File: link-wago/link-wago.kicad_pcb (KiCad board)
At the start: 4 copper layers, 70 x 29 mm, 37 parts, among them J101 2x05_Horizontal, J102 NE8FAH, J103 JAE_DX07S016JA3, J104 2x05_Horizontal, J105 NE8FAH, J106 Conn_01x01, J107 Conn_01x01, J108 WAGO-2065, J109 WAGO-2065, J110 WAGO-2065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

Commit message: Refresh
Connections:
- net /+24V-Supply renamed /+24V-Link
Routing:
- net GND: vias 29 -> 28

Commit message: Update
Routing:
- net GND: track 5.90 -> 12.1 mm, vias 28 -> 46
- net /Plug-RX-B: track 26.4 -> 25.7 mm
- net /USB-: track 36.8 -> 36.4 mm, vias 1 -> 2
- net /USB+: track 28.7 -> 28.5 mm, vias 1 -> 2
- added copper zone on B.Cu, net +5V
- removed copper zone on In2.Cu, net +24V
- removed copper zone on In2.Cu, net +5V
- removed copper zone on In2.Cu, net /+24V-Link

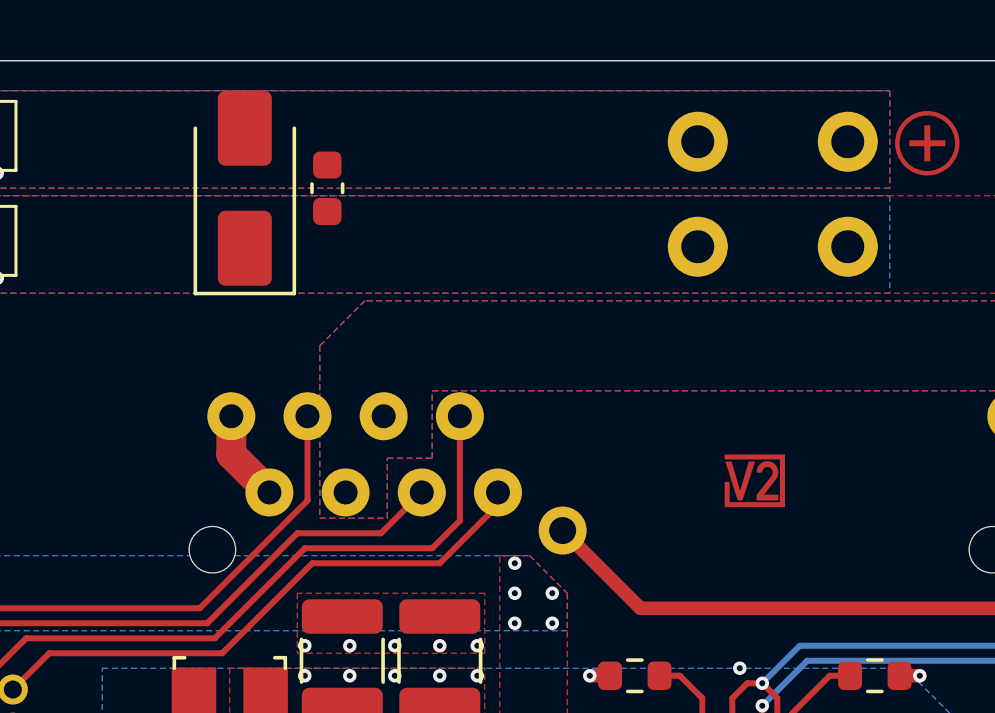
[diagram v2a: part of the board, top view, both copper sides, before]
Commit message: Update power symbols
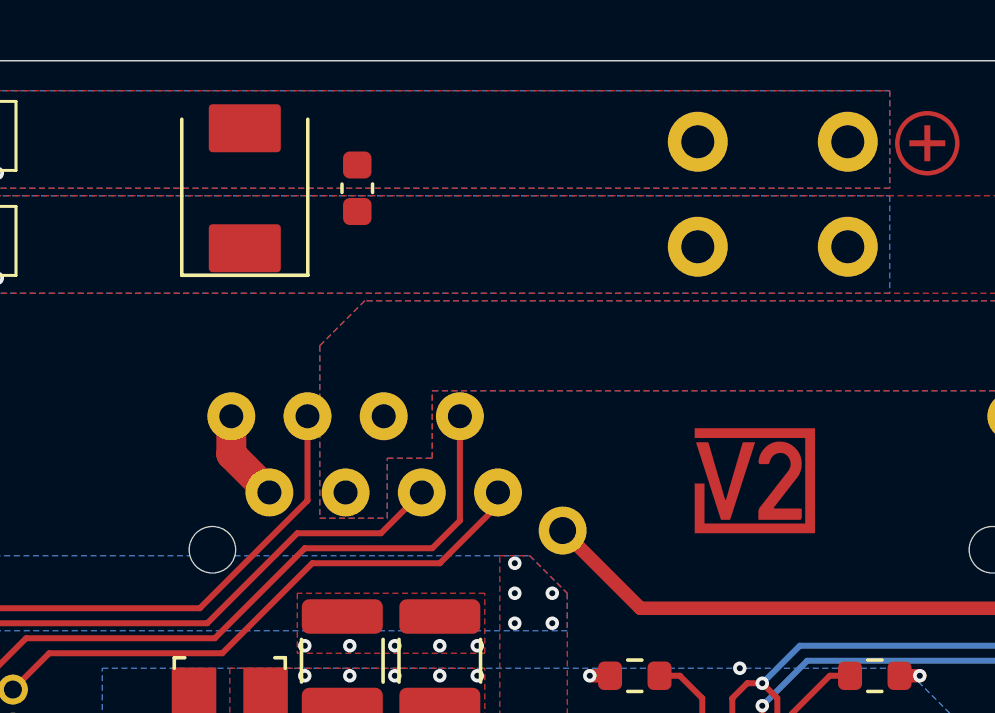
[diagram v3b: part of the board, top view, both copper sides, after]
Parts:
- C101, C502, C505: footprint Capacitor_SMD:C_0603_1608Metric -> V2_Capacitor_SMD:C_0603
- C501, C503, C504: footprint Capacitor_SMD:C_1210_3225Metric -> V2_Capacitor_SMD:C_1210
- FID101, FID102, FID103: value Fiducial -> Fiducial_Paste
- ICON102: footprint V2_Artwork:Logo_Tiny -> V2_Artwork:Logo_Small
- INFO102: value ORDER-NUMBER -> Order_Number
- J103: value JAE_DX07S016JA3 -> DX07S016JA3
- J106: value Conn_01x01 -> WAGO 2601-1101
- J107: renamed from J108; value WAGO-2065 -> WAGO 2065-100
- J108: renamed from J109; value WAGO-2065 -> WAGO 2065-100
- J109: renamed from J107; value Conn_01x01 -> WAGO 2601-1101
- J110, J111: value WAGO-2065 -> WAGO 2065-100
- R101, R102, R501, R502: footprint Resistor_SMD:R_0603_1608Metric -> V2_Resistor_SMD:R_0603
- TVS101: value SMAJ36CA -> SMBJ36CA; footprint Diode_SMD:D_SMA -> V2_Diode_SMD:D_SMB
- moved C101 1.00 mm to (138.8, 90.2)
- renumbered ICON106 to ICON105, ICON105 to ICON106
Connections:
- net USB-Shield renamed Shield

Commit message: Fix WAGOs
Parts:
- moved INFO101 4.50 mm to (123.5, 114.2)
- moved FID101 1.00 mm to (117.0, 114.0)
- moved FID102 1.00 mm to (117.0, 87.0)
- moved FID103 1.00 mm to (187.0, 114.0)
- moved ICON103 1.00 mm to (176.2, 88.5)
- moved ICON104 1.00 mm to (120.2, 95.5)
- moved ICON105 1.00 mm to (184.5, 113.5)
- moved ICON107 1.00 mm to (119.5, 113.5)
- moved J101 1.00 mm to (179.0, 109.5)
- moved J104 1.00 mm to (125.0, 109.5)
- moved J107 1.00 mm to (122.5, 88.5)
- moved J108 1.00 mm to (181.5, 88.5)
- moved J110 1.00 mm to (181.5, 92.0)
- moved J111 1.00 mm to (122.5, 92.0)
- moved PLUG101 1.00 mm to (179.0, 109.5)
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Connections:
- net /+24V-Link renamed +VLINK
- net VBUS renamed +VBUS
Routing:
- net /Socket-TX-Y: track 24.7 -> 25.7 mm
- net /USB-: track 36.4 -> 37.4 mm
- net /USB+: track 28.5 -> 29.5 mm
- net /Socket-TX-Z: track 27.5 -> 28.5 mm
- net /Socket-RX-B: track 22.0 -> 23.0 mm
- net /Plug-TX-Z: track 14.2 -> 15.2 mm
- net /Plug-TX-Y: track 11.8 -> 12.8 mm
- net /Socket-RX-A: track 19.7 -> 20.7 mm
- net /Plug-RX-A: track 16.8 -> 17.7 mm
- net /Plug-RX-B: track 25.7 -> 26.5 mm
- net GND: vias 46 -> 42
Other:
- board size 70 x 29 mm -> 72 x 29 mm

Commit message: Refresh
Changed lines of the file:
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@@
 			(effects
 				(font
-					(size 0.75 0.75)
+					(size 0.5 0.5)
 					(thickness 0.1)
 				)
@@
 			(effects
 				(font
-					(size 0.75 0.75)
+					(size 0.5 0.5)
 					(thickness 0.1)
 					(bold yes)
@@
 		)
 		(fp_line
-			(start -3.175 -1.2)
-			(end -3.175 -3.7)
-			(stroke
-				(width 0.127)
-				(type solid)
-			)
-			(layer "F.SilkS")
-		)
-		(fp_line
 			(start 3.175 -1.2)
 			(end -3.175 -1.2)
 			(stroke
-				(width 0.127)
+				(width 0.1)
 				(type solid)
 			)
@@
 			(end -2.54 -3.7)
 			(stroke
-				(width 0.127)
+				(width 0.1)
 				(type solid)
 			)
@@
 			(end -1.27 -3.7)
 			(stroke
-				(width 0.127)
+				(width 0.1)
 				(type solid)
 			)
@@
 			(end 2.54 -3.7)
 			(stroke
-				(width 0.127)
+				(width 0.1)
 				(type solid)
 			)
@@
 			(end 3.175 -3.7)
 			(stroke
-				(width 0.127)
+				(width 0.1)
 				(type solid)
 			)
 			(layer "F.SilkS")
 		)
-		(fp_line
-			(start 3.175 -3.7)
-			(end 3.175 -1.2)
+		(fp_poly
+			(pts
+				(xy 4.01 0.155) (xy 3.77 -0.175) (xy 4.25 -0.175) (xy 4.01 0.155)
+			)
 			(stroke
-				(width 0.127)
+				(width 0.12)
 				(type solid)
 			)
+			(fill yes)
 			(layer "F.SilkS")
 		)
@@
 			(effects
 				(font
-					(size 0.75 0.75)
+					(size 0.5 0.5)
 					(thickness 0.1)
 					(bold yes)
@@
 		)
 		(embedded_fonts no)
-		(model "../../3dmodels/V2_Connector_PinHeader_1.27mm.3dshapes/PinHeader_2x05_P1.27mm.stp"
+		(model "../../3dmodels/V2_Connector_PinHeader_1.27mm.3dshapes/PinHeader_2x05_P1.27mm_Horizontal.step"
 			(offset
 				(xyz 2.52 1.18 1.65)
@@
 				(font
 					(size 0.5 0.5)
-					(thickness 0.05)
+					(thickness 0.1)
+					(bold yes)
 				)
 			)
@@
 		)
 		(fp_line
-			(start 3.175 -3.7)
-			(end 3.175 -1.2)
-			(stroke
-				(width 0.127)
-				(type solid)
-			)
-			(layer "F.SilkS")
-		)
-		(fp_line
 			(start 2.54 -3.7)
 			(end 3.175 -3.7)
 			(stroke
-				(width 0.127)
+				(width 0.1)
 				(type solid)
 			)
@@
 			(end 2.54 -3.7)
 			(stroke
-				(width 0.127)
+				(width 0.1)
 				(type solid)
 			)
@@
 			(end -1.27 -3.7)
 			(stroke
-				(width 0.127)
+				(width 0.1)
 				(type solid)
 			)
@@
 			(end -2.54 -3.7)
 			(stroke
-				(width 0.127)
+				(width 0.1)
 				(type solid)
 			)
@@
 			(end -3.175 -1.2)
 			(stroke
-				(width 0.127)
+				(width 0.1)
 				(type solid)
 			)
 			(layer "F.SilkS")
 		)
-		(fp_line
-			(start -3.175 -1.2)
-			(end -3.175 -3.7)
+		(fp_poly
+			(pts
+				(xy 4.01 0.155) (xy 3.77 -0.175) (xy 4.25 -0.175) (xy 4.01 0.155)
+			)
 			(stroke
-				(width 0.127)
+				(width 0.12)
 				(type solid)
 			)
+			(fill yes)
 			(layer "F.SilkS")
 		)
@@
 			(effects
 				(font
-					(size 0.75 0.75)
+					(size 0.5 0.5)
 					(thickness 0.1)
 					(bold yes)
@@
 		)
 		(embedded_fonts no)
-		(model "../../3dmodels/V2_Connector_PinHeader_1.27mm.3dshapes/PinHeader_2x05_P1.27mm.stp"
+		(model "../../3dmodels/V2_Connector_PinHeader_1.27mm.3dshapes/PinHeader_2x05_P1.27mm_Horizontal.step"
 			(offset
 				(xyz 2.52 1.18 1.65)
@@
 			(effects
 				(font
-					(size 0.75 0.75)
+					(size 0.5 0.5)
 					(thickness 0.1)
 					(bold yes)
@@
 			(effects
 				(font
-					(size 0.75 0.75)
+					(size 0.5 0.5)
 					(thickness 0.1)
 					(bold yes)
@@
 			(effects
 				(font
-					(size 0.75 0.75)
+					(size 0.5 0.5)
 					(thickness 0.1)
 					(bold yes)
@@
 				(font
 					(size 0.5 0.5)
-					(thickness 0.05)
+					(thickness 0.1)
+					(bold yes)
 				)
 			)
@@
 			(effects
 				(font
-					(size 0.75 0.75)
+					(size 0.5 0.5)
 					(thickness 0.1)
 					(bold yes)
@@
 		)
 		(embedded_fonts no)
-		(model "/Users/kay/Documents/KiCad/9.0/versioduo.kicad/3dmodels/V2_Connector_WAGO.3dshapes/2601-1101.stp"
+		(model "../../3dmodels/V2_Connector_WAGO.3dshapes/2601-1101.stp"
 			(offset
 				(xyz 1.36 -1.9 0)
@@
 			(effects
 				(font
-					(size 0.75 0.75)
+					(size 0.5 0.5)
 					(thickness 0.1)
 					(bold yes)
@@
 		)
 		(embedded_fonts no)
-		(model "/Users/kay/Documents/KiCad/9.0/versioduo.kicad/3dmodels/V2_Connector_WAGO.3dshapes/2601-1101.stp"
+		(model "../../3dmodels/V2_Connector_WAGO.3dshapes/2601-1101.stp"
 			(offset
 				(xyz 1.36 -1.9 0)
@@
 			(effects
 				(font
-					(size 0.75 0.75)
+					(size 0.5 0.5)
 					(thickness 0.1)
 				)
@@
 			(effects
 				(font
-					(size 0.75 0.75)
+					(size 0.5 0.5)
 					(thickness 0.1)
 				)
@@
 	)
 	(gr_line
-		(start 188 87)
-		(end 188 106.25)
+		(start 116 87)
+		(end 116 106.25)
 		(stroke
 			(width 0.05)
@@
 		(layer "Edge.Cuts")
 	)
-	(gr_line
-		(start 116 112.75)
-		(end 116 114)
+	(gr_arc
+		(start 116 87)
+		(mid 116.292893 86.292893)
+		(end 117 86)
 		(stroke
 			(width 0.05)
@@
 	)
 	(gr_line
-		(start 117 86)
-		(end 187 86)
+		(start 116 112.75)
+		(end 116 114)
 		(stroke
 			(width 0.05)
@@
 	)
 	(gr_line
-		(start 116 87)
-		(end 116 106.25)
+		(start 117 86)
+		(end 187 86)
 		(stroke
 			(width 0.05)
@@
 		(layer "Edge.Cuts")
 	)
-	(gr_line
-		(start 188 112.75)
-		(end 188 114)
+	(gr_arc
+		(start 117 115)
+		(mid 116.292893 114.707107)
+		(end 116 114)
 		(stroke
 			(width 0.05)
@@
 		(layer "Edge.Cuts")
 	)
-	(gr_arc
+	(gr_line
 		(start 117 115)
-		(mid 116.292893 114.707107)
-		(end 116 114)
+		(end 187 115)
 		(stroke
 			(width 0.05)
@@
 	)
 	(gr_arc
-		(start 188 114)
-		(mid 187.707107 114.707107)
-		(end 187 115)
+		(start 187 86)
+		(mid 187.707107 86.292893)
+		(end 188 87)
 		(stroke
 			(width 0.05)
@@
 		(layer "Edge.Cuts")
 	)
-	(gr_arc
-		(start 116 87)
-		(mid 116.292893 86.292893)
-		(end 117 86)
+	(gr_line
+		(start 188 87)
+		(end 188 106.25)
 		(stroke
 			(width 0.05)
@@
 		(layer "Edge.Cuts")
 	)
-	(gr_arc
-		(start 187 86)
-		(mid 187.707107 86.292893)
-		(end 188 87)
+	(gr_line
+		(start 188 112.75)
+		(end 188 114)
 		(stroke
 			(width 0.05)
@@
 		(layer "Edge.Cuts")
 	)
-	(gr_line
-		(start 117 115)
+	(gr_arc
+		(start 188 114)
+		(mid 187.707107 114.707107)
 		(end 187 115)
 		(stroke

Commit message: Refresh
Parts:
- ICON104: value 24V -> ~; footprint V2_Artwork:24V -> V2_Artwork:28V
- TVS101: value SMBJ36CA -> SMBJ33CA
- moved ICON103 1.27 mm to (175.0, 88.8)
- moved ICON101 1.00 mm to (184.2, 95.5)
- moved ICON106 0.25 mm to (158.0, 88.8)
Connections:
- net +24V renamed +28V
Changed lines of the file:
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@@
 	(net 2 "/Power +5V/Feedback")
 	(net 3 "+5V")
-	(net 4 "+24V")
+	(net 4 "+28V")
 	(net 5 "/Power +5V/Vcc")
 	(net 6 "+VLINK")
@@
 			(size 4.6 2)
 			(layers "F.Cu" "F.Mask")
-			(net 4 "+24V")
+			(net 4 "+28V")
 			(pintype "passive")
 			(zone_connect 2)
@@
 			)
 		)
-		(property "Value" "SMBJ36CA"
+		(property "Value" "SMBJ33CA"
 			(at 0 3.1 90)
 			(layer "F.Fab")
@@
 			(layers "F.Cu" "F.Mask" "F.Paste")
 			(roundrect_rratio 0.07692307692)
-			(net 4 "+24V")
+			(net 4 "+28V")
 			(pinfunction "A")
 			(pintype "passive")
@@
 			(layers "F.Cu" "F.Mask" "F.Paste")
 			(roundrect_rratio 0.1428571429)
-			(net 4 "+24V")
+			(net 4 "+28V")
 			(pintype "passive")
 		)
@@
 	(footprint "V2_Artwork:Plus_Small"
 		(layer "F.Cu")
-		(at 157.75 88.75 90)
+		(at 158 88.75 90)
 		(property "Reference" "ICON106"
 			(at 0 -2.5 90)
@@
 		(embedded_fonts no)
 	)
-	(footprint "V2_Artwork:24V"
+	(footprint "V2_Artwork:28V"
 		(layer "F.Cu")
 		(at 120.25 95.5)
@@
 			)
 		)
-		(property "Value" "24V"
+		(property "Value" "~"
 			(at 0 2.5 0)
 			(unlocked yes)
@@
 		(sheetfile "link-wago.kicad_sch")
 		(attr exclude_from_pos_files exclude_from_bom allow_missing_courtyard)
-		(fp_text user "24V"
+		(fp_text user "28V"
 			(at 0 0 0)
 			(unlocked yes)
@@
 			)
 		)
-		(fp_text user "24V"
+		(fp_text user "28V"
 			(at 0 0 0)
 			(unlocked yes)
@@
 	(footprint "V2_Artwork:5V"
 		(layer "F.Cu")
-		(at 183.25 95.5)
+		(at 184.25 95.5)
 		(property "Reference" "ICON101"
 			(at 0 -2.5 0)
@@
 			(layers "F.Cu" "F.Mask" "F.Paste")
 			(roundrect_rratio 0.09090909091)
-			(net 4 "+24V")
+			(net 4 "+28V")
 			(pintype "passive")
 		)
@@
 			(layers "F.Cu" "F.Mask" "F.Paste")
 			(roundrect_rratio 0.1428571429)
-			(net 4 "+24V")
+			(net 4 "+28V")
 			(pintype "passive")
 		)
@@
 			(layers "F.Cu" "F.Mask" "F.Paste")
 			(roundrect_rratio 0.15)
-			(net 4 "+24V")
+			(net 4 "+28V")
 			(pinfunction "EN")
 			(pintype "input")
@@
 			(layers "F.Cu" "F.Mask" "F.Paste")
 			(roundrect_rratio 0.15)
-			(net 4 "+24V")
+			(net 4 "+28V")
 			(pinfunction "VIN")
 			(pintype "power_in")
@@
 	(footprint "V2_Artwork:Plus_Small"
 		(layer "F.Cu")
-		(at 176.25 88.5 -90)
+		(at 175 88.75 -90)
 		(property "Reference" "ICON103"
 			(at 0 -2.5 270)
@@
 			(keep_end_layers yes)
 			(zone_layer_connections)
-			(net 4 "+24V")
+			(net 4 "+28V")
 			(pintype "passive")
 		)
@@
 			(keep_end_layers yes)
 			(zone_layer_connections)
-			(net 4 "+24V")
+			(net 4 "+28V")
 			(pintype "passive")
 		)
@@
 		(layer "F.Cu")
 		(hatch edge 0.5)
-		(priority 2)
 		(connect_pads yes
 			(clearance 0.2)
@@
 		(layer "F.Cu")
 		(hatch edge 0.5)
-		(priority 2)
 		(connect_pads yes
 			(clearance 0.2)
@@
 	(zone
 		(net 4)
-		(net_name "+24V")
+		(net_name "+28V")
 		(layer "F.Cu")
 		(hatch edge 0.5)
-		(priority 1)
 		(connect_pads yes
 			(clearance 0.2)
@@
 	(zone
 		(net 4)
-		(net_name "+24V")
+		(net_name "+28V")
 		(layer "F.Cu")
 		(hatch edge 0.5)
-		(priority 8)
 		(connect_pads yes
 			(clearance 0.2)
@@
 		(layer "F.Cu")
 		(hatch edge 0.5)
-		(priority 2)
 		(connect_pads yes
 			(clearance 0.2)
@@
 		(layer "F.Cu")
 		(hatch edge 0.5)
-		(priority 3)
 		(connect_pads yes
 			(clearance 0.2)
@@
 		(layers "F.Cu" "B.Cu")
 		(hatch edge 0.5)
-		(priority 7)
 		(connect_pads yes
 			(clearance 0.2)
@@
 	(zone
 		(net 4)
-		(net_name "+24V")
+		(net_name "+28V")
 		(layer "B.Cu")
 		(hatch edge 0.5)

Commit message: Add comment
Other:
- board text added: "Move WAGOs further in"
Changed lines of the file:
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@@
 		(layer "Edge.Cuts")
+	)
+	(gr_text "Move WAGOs further in"
+		(at 116.25 75.5 0)
+		(layer "F.Fab")
+		(effects
+			(font
+				(size 1 1)
+				(thickness 0.15)
+			)
+			(justify left bottom)
+		)
 	)
 	(segment
